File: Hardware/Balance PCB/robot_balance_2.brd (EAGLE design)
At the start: 100 x 50 mm, 58 parts, among them P1 10118194-0001LF, Q1 16Mhz

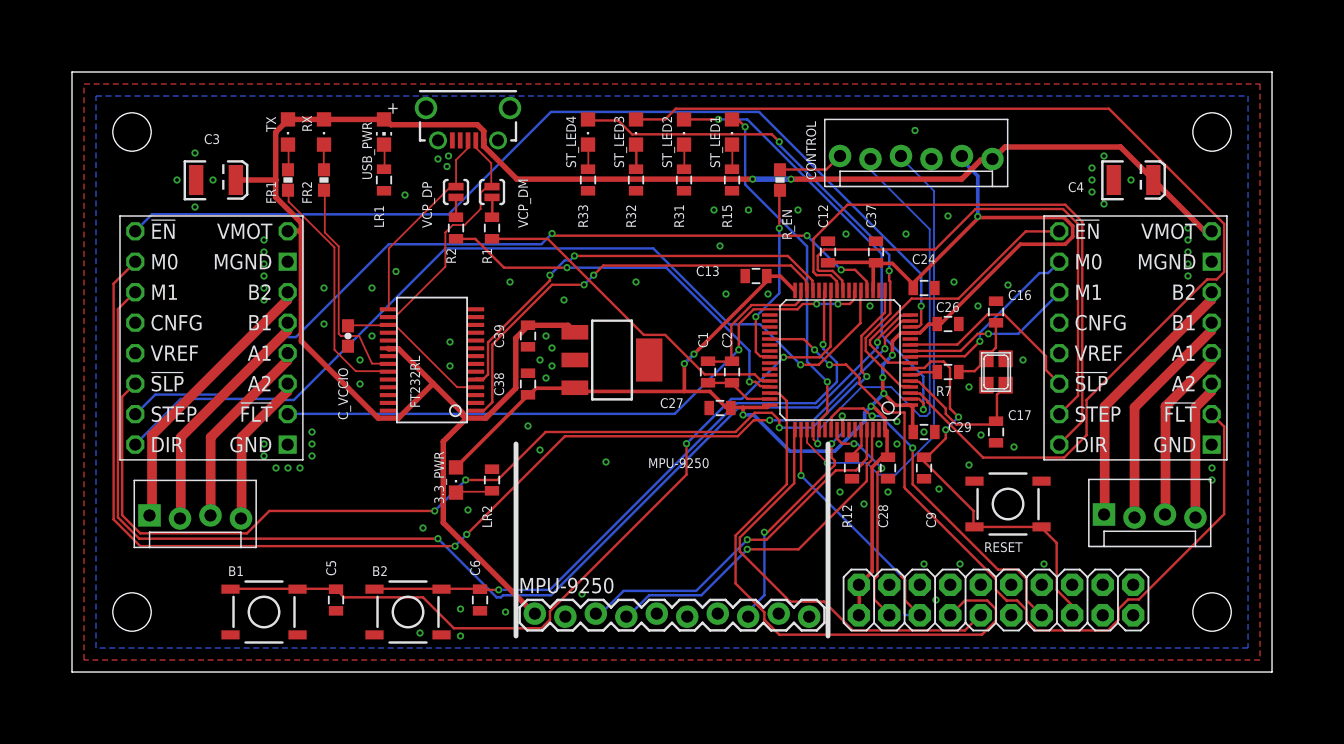
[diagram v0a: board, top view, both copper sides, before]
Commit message: Work on stepper motor driver and matlab
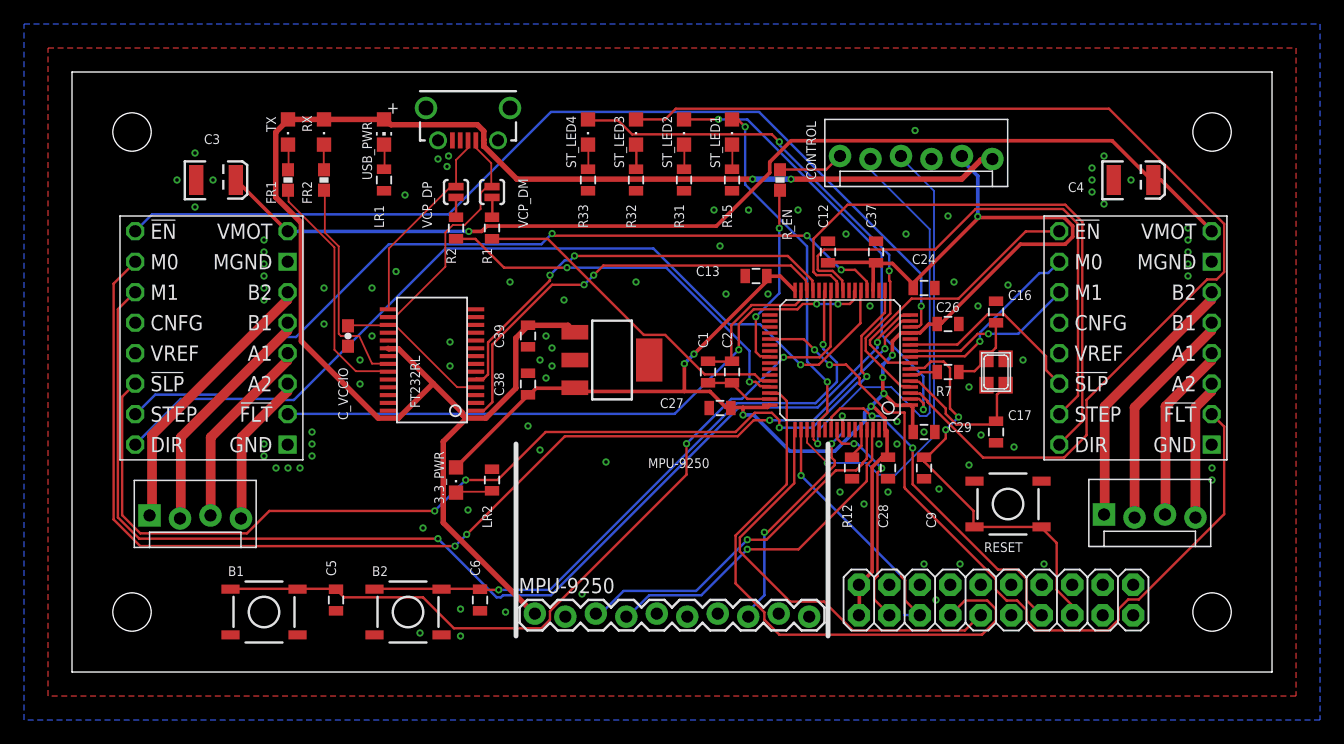
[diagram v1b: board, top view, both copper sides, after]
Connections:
- new net V_USB: C3.A, C4.A, U$1.16, U$3.16
- net 5V: no longer C3.A, C4.A, U$1.16, U$3.16
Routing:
- net V_USB: track 0.00 -> 89.9 mm, vias 0 -> 1
- net 5V: track 167.1 -> 141.0 mm
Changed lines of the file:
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@@
 <layer number="27" name="tValues" color="7" fill="1" visible="yes" active="yes"/>
 <layer number="28" name="bValues" color="7" fill="1" visible="yes" active="yes"/>
-<layer number="29" name="tStop" color="7" fill="3" visible="no" active="yes"/>
-<layer number="30" name="bStop" color="7" fill="6" visible="no" active="yes"/>
-<layer number="31" name="tCream" color="7" fill="4" visible="no" active="yes"/>
-<layer number="32" name="bCream" color="7" fill="5" visible="no" active="yes"/>
+<layer number="29" name="tStop" color="7" fill="3" visible="yes" active="yes"/>
+<layer number="30" name="bStop" color="7" fill="6" visible="yes" active="yes"/>
+<layer number="31" name="tCream" color="7" fill="4" visible="yes" active="yes"/>
+<layer number="32" name="bCream" color="7" fill="5" visible="yes" active="yes"/>
 <layer number="33" name="tFinish" color="6" fill="3" visible="no" active="yes"/>
 <layer number="34" name="bFinish" color="6" fill="6" visible="no" active="yes"/>
@@
 </class>
 </classes>
-<designrules name="ITEADstudio_DRC *">
+<designrules name="ITEADstudio_DRC">
 <description language="de">&lt;b&gt;EAGLE Design Rules&lt;/b&gt;
 &lt;p&gt;
@@
 <param name="rvMicroViaOuter" value="0.25"/>
 <param name="rvMicroViaInner" value="0.25"/>
-<param name="rlMinPadTop" value="5mil"/>
+<param name="rlMinPadTop" value="10mil"/>
 <param name="rlMaxPadTop" value="20mil"/>
 <param name="rlMinPadInner" value="10mil"/>
 <param name="rlMaxPadInner" value="20mil"/>
-<param name="rlMinPadBottom" value="5mil"/>
+<param name="rlMinPadBottom" value="10mil"/>
 <param name="rlMaxPadBottom" value="20mil"/>
 <param name="rlMinViaOuter" value="6mil"/>
@@
 <param name="RoutingGrid" value="50mil"/>
 <param name="AutoGrid" value="1"/>
-<param name="Efforts" value="2"/>
+<param name="Efforts" value="0"/>
 <param name="TopRouterVariant" value="1"/>
 <param name="tpViaShape" value="round"/>
@@
 <contactref element="C4" pad="C"/>
 <polygon width="0.1524" layer="1">
-<vertex x="1" y="49"/>
-<vertex x="99" y="49"/>
-<vertex x="99" y="1"/>
-<vertex x="1" y="1"/>
+<vertex x="-2" y="52"/>
+<vertex x="102" y="52"/>
+<vertex x="102" y="-2"/>
+<vertex x="-2" y="-2"/>
 </polygon>
 <polygon width="0.1524" layer="16">
-<vertex x="2" y="48"/>
-<vertex x="98" y="48"/>
-<vertex x="98" y="2"/>
-<vertex x="2" y="2"/>
+<vertex x="-4" y="54"/>
+<vertex x="104" y="54"/>
+<vertex x="104" y="-4"/>
+<vertex x="-4" y="-4"/>
 </polygon>
 <contactref element="U$4" pad="12"/>
@@
 <via x="55.9181" y="21.4249" extent="1-16" drill="0.3048"/>
 </signal>
+<signal name="V_USB" class="3">
+<contactref element="U$1" pad="16"/>
+<contactref element="C3" pad="A"/>
+<contactref element="U$3" pad="16"/>
+<contactref element="C4" pad="A"/>
+<wire x1="17.9578" y1="36.7157" x2="13.6906" y2="40.9829" width="0.3048" layer="1"/>
+<wire x1="13.6906" y1="40.9829" x2="13.65" y2="41" width="0.3048" layer="1"/>
+<wire x1="17.9578" y1="36.7157" x2="17.97" y2="36.73" width="0.3048" layer="1"/>
+<wire x1="90.7669" y1="40.9829" x2="90.1446" y2="40.9829" width="0.3048" layer="1"/>
+<wire x1="94.9452" y1="36.8046" x2="90.7669" y2="40.9829" width="0.3048" layer="1"/>
+<wire x1="90.1446" y1="40.9829" x2="90.11" y2="41" width="0.3048" layer="1"/>
+<wire x1="94.9452" y1="36.8046" x2="94.97" y2="36.73" width="0.3048" layer="1"/>
+<wire x1="33.0708" y1="36.7157" x2="18.0467" y2="36.7157" width="0.3048" layer="16"/>
+<wire x1="34.1376" y1="36.7157" x2="33.0708" y2="36.7157" width="0.3048" layer="1"/>
+<wire x1="34.5821" y1="37.1602" x2="34.1376" y2="36.7157" width="0.3048" layer="1"/>
+<wire x1="53.6956" y1="37.1602" x2="34.5821" y2="37.1602" width="0.3048" layer="1"/>
+<wire x1="58.1406" y1="41.6052" x2="53.6956" y2="37.1602" width="0.3048" layer="1"/>
+<wire x1="58.1406" y1="42.4942" x2="58.1406" y2="41.6052" width="0.3048" layer="1"/>
+<wire x1="59.9186" y1="44.2722" x2="58.1406" y2="42.4942" width="0.3048" layer="1"/>
+<wire x1="86.6775" y1="44.2722" x2="59.9186" y2="44.2722" width="0.3048" layer="1"/>
+<wire x1="89.9668" y1="40.9829" x2="86.6775" y2="44.2722" width="0.3048" layer="1"/>
+<wire x1="18.0467" y1="36.7157" x2="17.97" y2="36.73" width="0.3048" layer="16"/>
+<wire x1="89.9668" y1="40.9829" x2="90.11" y2="41" width="0.3048" layer="1"/>
+<via x="33.0708" y="36.7157" extent="1-16" drill="0.3048"/>
+</signal>
 <signal name="N$18" class="1">
 <contactref element="3.3_PWR" pad="C"/>
@@
 <wire x1="25.5143" y1="21.1582" x2="27.2034" y2="21.1582" width="0.4572" layer="1"/>
 <wire x1="19.1135" y1="27.559" x2="25.5143" y2="21.1582" width="0.4572" layer="1"/>
-<wire x1="19.1135" y1="37.4269" x2="19.1135" y2="36.75" width="0.4572" layer="1"/>
-<wire x1="19.1135" y1="36.75" x2="19.1135" y2="27.559" width="0.4572" layer="1"/>
+<wire x1="19.1135" y1="37.4269" x2="19.1135" y2="27.559" width="0.4572" layer="1"/>
 <wire x1="16.9799" y1="39.5605" x2="19.1135" y2="37.4269" width="0.4572" layer="1"/>
-<wire x1="16.9799" y1="44.9834" x2="16.9799" y2="41" width="0.4572" layer="1"/>
-<wire x1="16.9799" y1="41" x2="16.9799" y2="39.5605" width="0.4572" layer="1"/>
+<wire x1="16.9799" y1="44.9834" x2="16.9799" y2="39.5605" width="0.4572" layer="1"/>
 <wire x1="17.8689" y1="45.8724" x2="16.9799" y2="44.9834" width="0.4572" layer="1"/>
 <wire x1="17.8689" y1="45.8724" x2="18" y2="46.05" width="0.4572" layer="1"/>
 <via x="59.9186" y="41.0718" extent="1-16" drill="0.3048"/>
 <via x="56.7182" y="41.0718" extent="1-16" drill="0.3048"/>
-<contactref element="C4" pad="A"/>
-<contactref element="U$3" pad="16"/>
-<contactref element="C3" pad="A"/>
-<contactref element="U$1" pad="16"/>
-<wire x1="16.9799" y1="41" x2="13.65" y2="41" width="0.4572" layer="1"/>
-<wire x1="19.1135" y1="36.75" x2="18" y2="36.75" width="0.4572" layer="1"/>
-<wire x1="18" y1="36.75" x2="17.97" y2="36.73" width="0.4572" layer="1"/>
-<wire x1="94.375" y1="36.75" x2="90.125" y2="41" width="0.4572" layer="1"/>
-<wire x1="94.875" y1="36.75" x2="94.375" y2="36.75" width="0.4572" layer="1"/>
-<wire x1="90.125" y1="41" x2="90.11" y2="41" width="0.4572" layer="1"/>
-<wire x1="94.875" y1="36.75" x2="94.97" y2="36.73" width="0.4572" layer="1"/>
-<wire x1="77.75" y1="43.75" x2="76.875" y2="42.875" width="0.4572" layer="1"/>
-<wire x1="87.375" y1="43.75" x2="77.75" y2="43.75" width="0.4572" layer="1"/>
-<wire x1="90" y1="41.125" x2="87.375" y2="43.75" width="0.4572" layer="1"/>
-<wire x1="76.875" y1="42.875" x2="76.7" y2="42.746" width="0.4572" layer="1"/>
-<wire x1="90" y1="41.125" x2="90.11" y2="41" width="0.4572" layer="1"/>
 </signal>
 <signal name="N$9" class="1">
